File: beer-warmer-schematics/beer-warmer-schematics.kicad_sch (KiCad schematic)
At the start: 20 parts, among them J1 USB_C_Receptacle_USB2.0_14P, J2 Screw_Terminal_01x02, J3 Conn_01x07_Socket, J4 Conn_01x07_Socket, J5 Conn_01x04_Pin, J6 Screw_Terminal_01x03, Q1 AOD4184A, U2 LM2596S-5, U3 CH224K

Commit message: initial routing
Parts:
- added FID1, FID2, FID3: Fiducial, Fiducial:Fiducial_0.5mm_Mask1.5mm, symbol Mechanical:Fiducial
- added H1, H2, H3, H4: MountingHole, MountingHole:MountingHole_3.2mm_M3, symbol Mechanical:MountingHole
- added R5: 10K, Resistor_SMD:R_0201_0603Metric, symbol Device:R
- U1: footprint (none) -> Library:XIAO-ESP32C6-DIP
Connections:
- net +5V: now also U1.14 (5V); no longer U1.13 (5V)
- net D0: now also U1.1 (D0); no longer U1.0 (D0)
- net D1: now also U1.2 (D1); no longer U1.1 (D1)
- net GND: now also U1.13 (GND); no longer U1.12 (GND), U3.8 (VBUS)
- net SCL: now also U1.6 (D5); no longer U1.5 (D5)
- net SDA: now also U1.5 (D4); no longer U1.4 (D4)
- net at U1.10 (D9): now also J3.5 (Pin_5); no longer J3.4 (Pin_4)
- net at U1.11 (D10): now also J3.4 (Pin_4); no longer J3.3 (Pin_3)
- net at U1.3 (D2): now also J4.5 (Pin_5); no longer J4.4 (Pin_4)
- net at J4.1 (Pin_1): now also U1.7 (D6); no longer U1.6 (D6)
- net at J3.7 (Pin_7): now also U1.8 (D7); no longer U1.7 (D7)
- net at J3.6 (Pin_6): now also U1.9 (D8); no longer U1.8 (D8)
- net at J1.A4 (VBUS), J1.A9 (VBUS), J1.B4 (VBUS)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: now also R5.1
- new net: R5.2, U3.8 (VBUS)
- new net: J3.3 (Pin_3), U1.12 (3V3)
- new net: J4.4 (Pin_4), U1.4 (D3)
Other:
- moved on the sheet: C1, R1

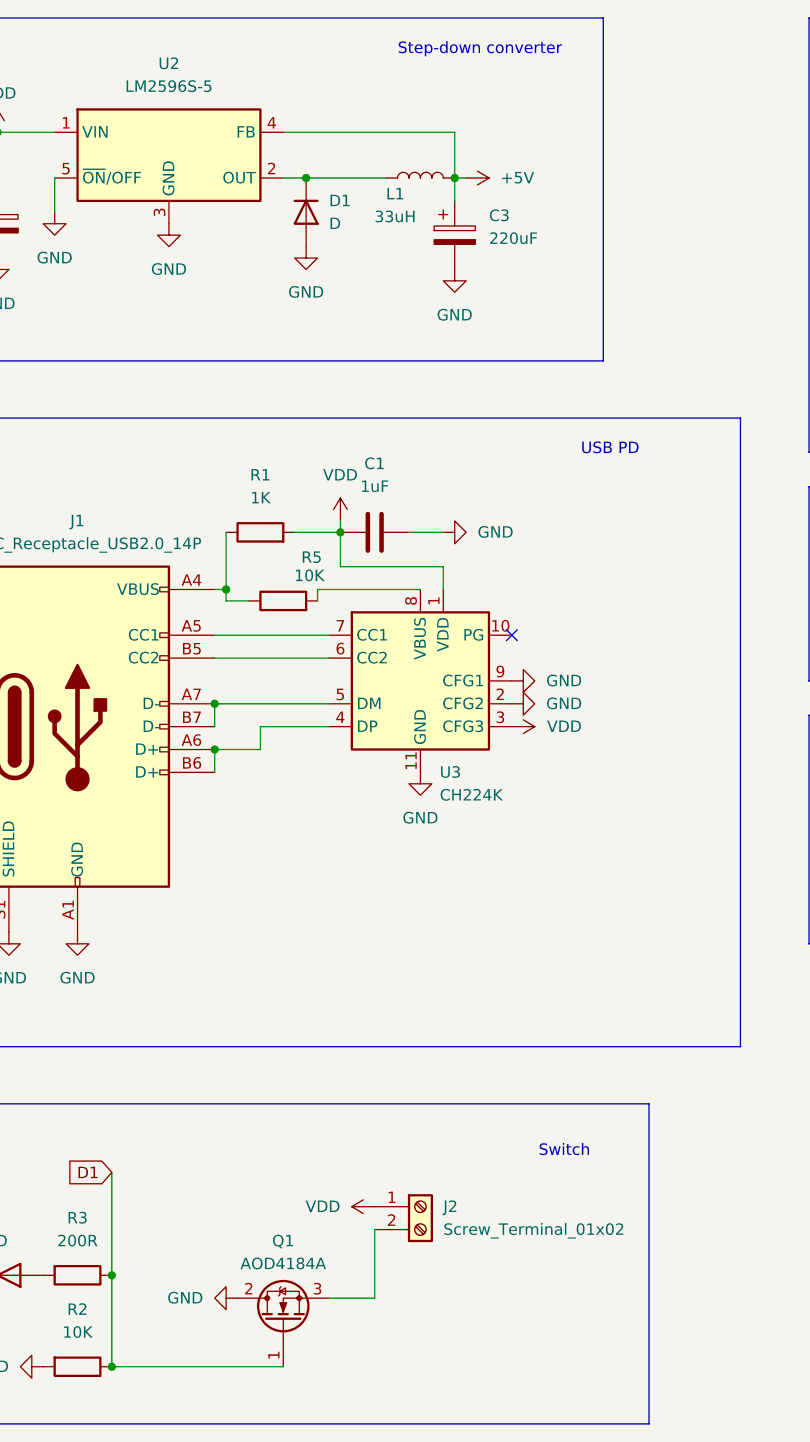
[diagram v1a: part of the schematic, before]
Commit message: cleanup add more lcsc numbers
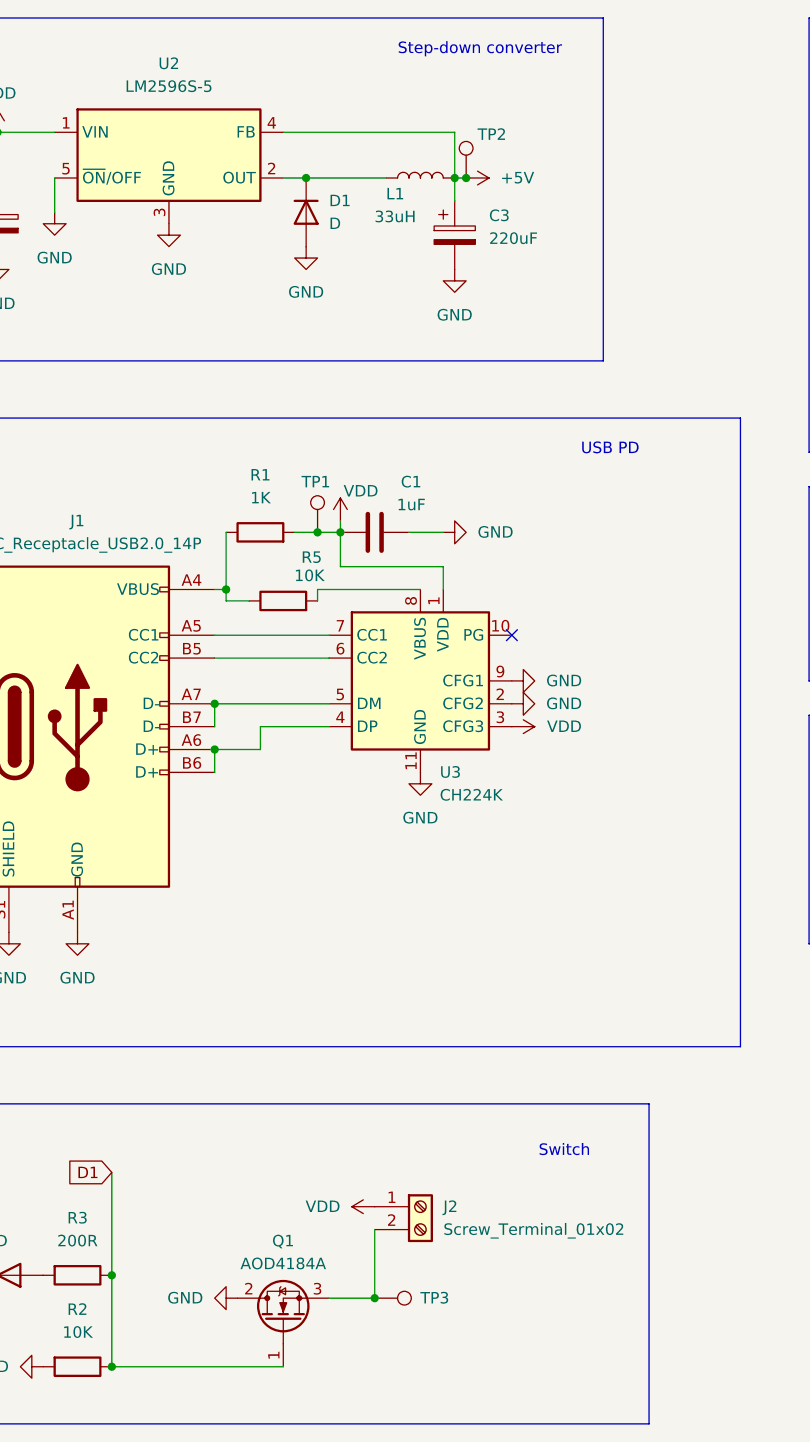
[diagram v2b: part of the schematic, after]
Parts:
- added TP1, TP2, TP3: TestPoint, TestPoint:TestPoint_Pad_D1.0mm, symbol Connector:TestPoint
- D2: LCSC (none) -> C2286
- J3, J4: LCSC (none) -> C2932672
- J5: LCSC (none) -> C594232
- Q1: LCSC (none) -> C99124
- R1: LCSC (none) -> C22548
- R3: LCSC C15401 -> C8218
- U2: LCSC (none) -> C5276750
- U3: LCSC (none) -> C970725
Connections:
- net +5V: now also TP2.1
- net VDD: now also TP1.1
- net at J2.2 (Pin_2), Q1.3 (S): now also TP3.1

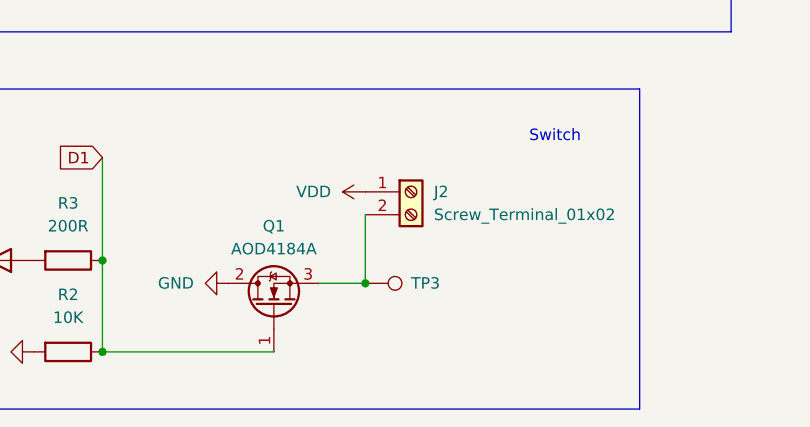
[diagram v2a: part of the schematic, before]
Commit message: redid board layout
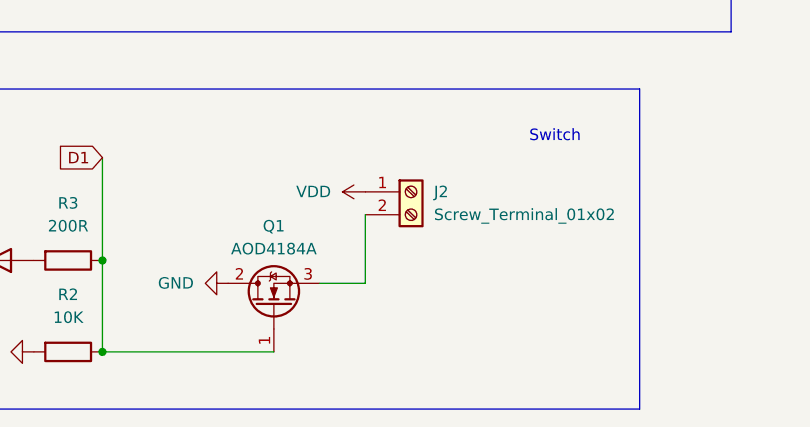
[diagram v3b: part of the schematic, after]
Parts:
- removed TP3: TestPoint, TestPoint:TestPoint_Pad_D1.0mm, symbol Connector:TestPoint
- H1, H2, H3, H4: footprint MountingHole:MountingHole_3.2mm_M3 -> MountingHole:MountingHole_3.2mm_M3_DIN965_Pad
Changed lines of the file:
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@@
 	)
 	(junction
-		(at 83.82 160.02)
-		(diameter 0)
-		(color 0 0 0 0)
-	)
-	(junction
 		(at 41.91 30.48)
 		(diameter 0)
@@
 	)
 	(symbol
-		(lib_id "Connector:TestPoint")
-		(at 83.82 160.02 270)
-		(unit 1)
-		(exclude_from_sim no)
-		(in_bom yes)
-		(on_board yes)
-		(dnp no)
-		(property "Reference" "TP3"
-			(at 88.9 160.02 90)
-			(effects
-				(font
-					(size 1.27 1.27)
-				)
-				(justify left)
-			)
-		)
-		(property "Value" "TestPoint"
-			(at 88.9 161.2899 90)
-			(effects
-				(font
-					(size 1.27 1.27)
-				)
-				(justify left)
-				(hide yes)
-			)
-		)
-		(property "Footprint" "TestPoint:TestPoint_Pad_D1.0mm"
-			(at 83.82 165.1 0)
-			(effects
-				(font
-					(size 1.27 1.27)
-				)
-				(hide yes)
-			)
-		)
-		(property "Datasheet" "~"
-			(at 83.82 165.1 0)
-			(effects
-				(font
-					(size 1.27 1.27)
-				)
-				(hide yes)
-			)
-		)
-		(property "Description" "test point"
-			(at 83.82 160.02 0)
-			(effects
-				(font
-					(size 1.27 1.27)
-				)
-				(hide yes)
-			)
-		)
-		(pin "1"
-		)
-		(instances
-			(project ""
-				(path "/70572ac2-8723-48b8-abb1-12d225a3bb68"
-					(reference "TP3")
-					(unit 1)
-				)
-			)
-		)
-	)
-	(symbol
 		(lib_id "power:GND")
 		(at 143.51 100.33 270)
@@
 			)
 		)
-		(property "Footprint" "MountingHole:MountingHole_3.2mm_M3"
+		(property "Footprint" "MountingHole:MountingHole_3.2mm_M3_DIN965_Pad"
 			(at 208.28 111.76 0)
 			(effects
@@
 			)
 		)
-		(property "Footprint" "MountingHole:MountingHole_3.2mm_M3"
+		(property "Footprint" "MountingHole:MountingHole_3.2mm_M3_DIN965_Pad"
 			(at 208.28 105.41 0)
 			(effects
@@
 			)
 		)
-		(property "Footprint" "MountingHole:MountingHole_3.2mm_M3"
+		(property "Footprint" "MountingHole:MountingHole_3.2mm_M3_DIN965_Pad"
 			(at 208.28 92.71 0)
 			(effects
@@
 			)
 		)
-		(property "Footprint" "MountingHole:MountingHole_3.2mm_M3"
+		(property "Footprint" "MountingHole:MountingHole_3.2mm_M3_DIN965_Pad"
 			(at 208.28 99.06 0)
 			(effects

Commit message: fix screw terminal component
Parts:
- J2: footprint TerminalBlock_Phoenix:TerminalBlock_Phoenix_MKDS-1,5-2_1x02_P5.00mm_Horizontal -> TerminalBlock_Phoenix:TerminalBlock_Phoenix_MKDS-1,5-2-5.08_1x02_P5.08mm_Horizontal; LCSC C128027 -> C8465
- J6: footprint TerminalBlock_Phoenix:TerminalBlock_Phoenix_MKDS-1,5-3_1x03_P5.00mm_Horizontal -> TerminalBlock_Phoenix:TerminalBlock_Phoenix_MKDS-1,5-3-5.08_1x03_P5.08mm_Horizontal; LCSC C128026 -> C72334
- TP1, TP2: now left out of the parts list
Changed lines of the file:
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@@
 		(unit 1)
 		(exclude_from_sim no)
-		(in_bom yes)
+		(in_bom no)
 		(on_board yes)
 		(dnp no)
@@
 		(unit 1)
 		(exclude_from_sim no)
-		(in_bom yes)
+		(in_bom no)
 		(on_board yes)
 		(dnp no)
@@
 			)
 		)
-		(property "Footprint" "TerminalBlock_Phoenix:TerminalBlock_Phoenix_MKDS-1,5-2_1x02_P5.00mm_Horizontal"
+		(property "Footprint" "TerminalBlock_Phoenix:TerminalBlock_Phoenix_MKDS-1,5-2-5.08_1x02_P5.08mm_Horizontal"
 			(at 88.9 149.86 0)
 			(effects
@@
 			)
 		)
-		(property "LCSC" "C128027"
+		(property "LCSC" "C8465"
 			(at 88.9 149.86 0)
 			(effects
@@
 			)
 		)
-		(property "Footprint" "TerminalBlock_Phoenix:TerminalBlock_Phoenix_MKDS-1,5-3_1x03_P5.00mm_Horizontal"
+		(property "Footprint" "TerminalBlock_Phoenix:TerminalBlock_Phoenix_MKDS-1,5-3-5.08_1x03_P5.08mm_Horizontal"
 			(at 158.75 102.87 0)
 			(effects
@@
 			)
 		)
-		(property "LCSC" "C128026"
+		(property "LCSC" "C72334"
 			(at 158.75 102.87 0)
 			(effects

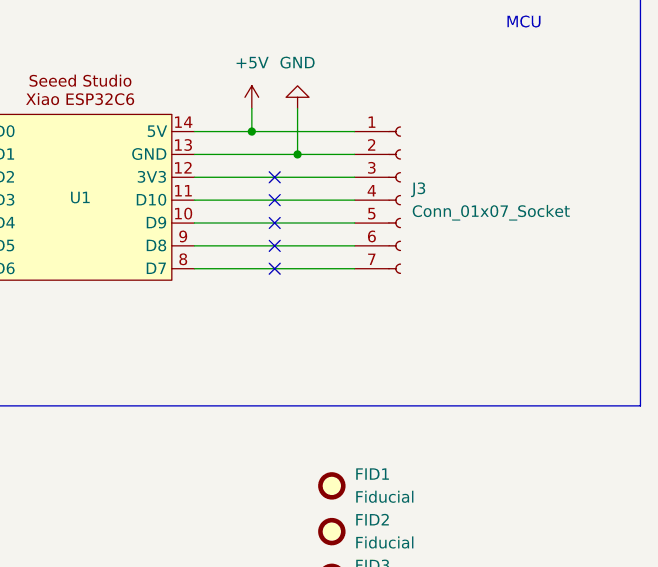
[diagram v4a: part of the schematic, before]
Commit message: power indicator
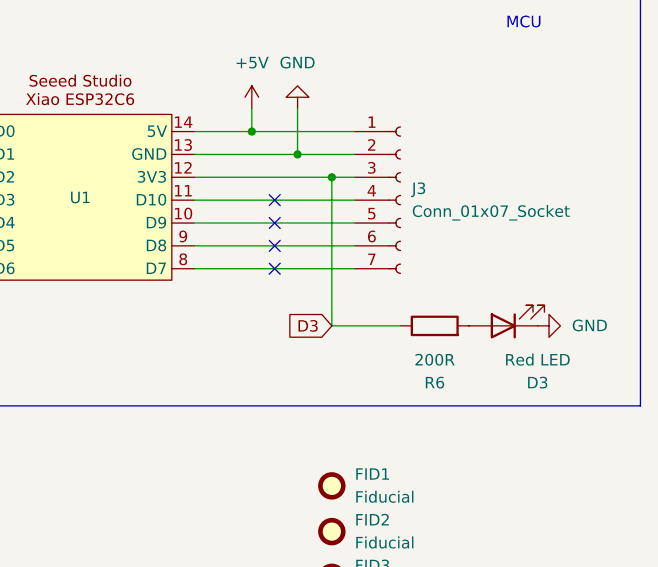
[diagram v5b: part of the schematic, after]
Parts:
- added D3: Red LED, Resistor_SMD:R_0201_0603Metric, symbol Device:LED
- added R6: 200R, Resistor_SMD:R_0201_0603Metric, symbol Device:R
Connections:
- net GND: now also D3.1 (K)
- net D3: now reaches J3.3 (Pin_3), U1.12 (3V3)
- net D3: now also R6.1
- new net: D3.2 (A), R6.2
- no-connect marks 9 -> 8

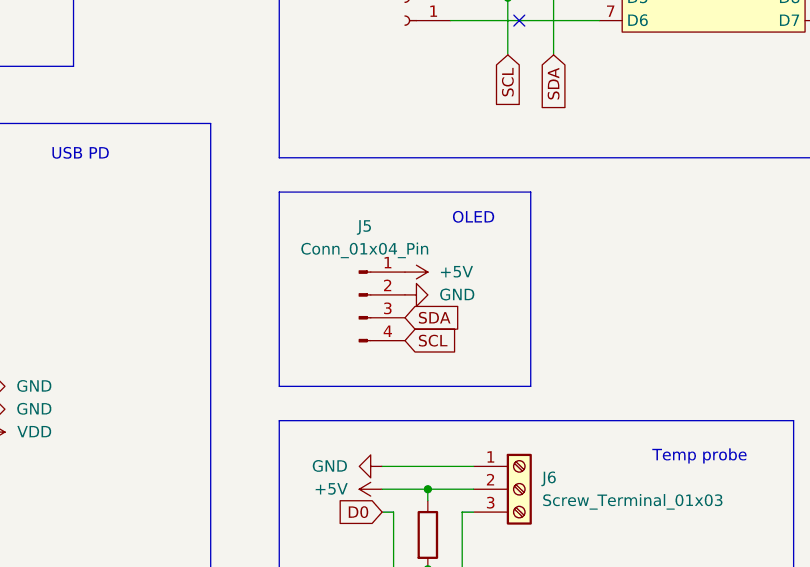
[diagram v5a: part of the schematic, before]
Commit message: use more standard components
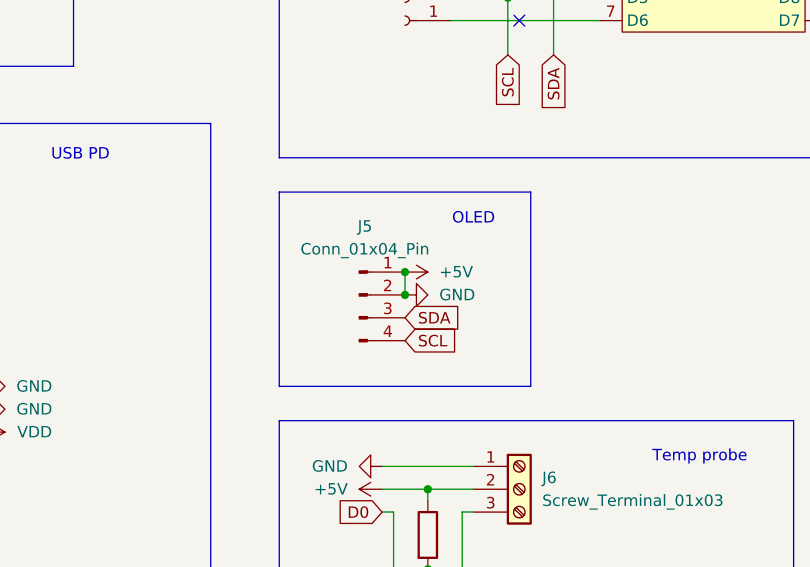
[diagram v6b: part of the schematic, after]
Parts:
- C1: footprint Capacitor_SMD:C_0201_0603Metric -> Capacitor_SMD:CP_Elec_10x10.5; LCSC C1592 -> C7471898
- C2: footprint Capacitor_THT:CP_Radial_D10.0mm_P5.00mm -> Capacitor_SMD:CP_Elec_10x10.5; LCSC C323859 -> C7471898
- C3: footprint Capacitor_THT:CP_Radial_D6.3mm_P2.50mm -> Capacitor_SMD:CP_Elec_6.3x7.7; LCSC C43340 -> C3342
- D1: LCSC C2102 -> C8598
- L1: footprint Library:IND_BOURNS_SRR1280 -> Inductor_SMD:L_SXN_SMDRI127; LCSC C2045204 -> C9400
- R1: footprint Resistor_SMD:R_0201_0603Metric -> Resistor_SMD:R_1206_3216Metric; LCSC C22548 -> C4410
- R2, R4, R5: footprint Resistor_SMD:R_0201_0603Metric -> Resistor_SMD:R_1206_3216Metric; LCSC C15401 -> C17902
- R3, R6: LCSC C8218 -> C22962
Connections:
- net GND is gone; now on net +5V: C1.2, C2.2, C3.2, D1.2 (A), D2.1 (K), D3.1 (K), J1.A1 (GND), J1.A12 (GND), J1.B1 (GND), J1.B12 (GND), J1.S1 (SHIELD), J3.2 (Pin_2), J5.2 (Pin_2), J6.1 (Pin_1), Q1.2 (D), R2.2, U1.13 (GND), U2.3 (GND), U2.5 (~{ON}/OFF), U3.11 (GND), U3.2 (CFG2), U3.9 (CFG1)
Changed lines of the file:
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@@
 	)
 	(junction
+		(at 146.05 78.74)
+		(diameter 0)
+		(color 0 0 0 0)
+	)
+	(junction
 		(at 157.48 35.56)
 		(diameter 0)
@@
 	)
 	(junction
+		(at 146.05 81.28)
+		(diameter 0)
+		(color 0 0 0 0)
+	)
+	(junction
 		(at 199.39 35.56)
 		(diameter 0)
@@
 	(wire
 		(pts
+			(xy 146.05 78.74) (xy 146.05 81.28)
+		)
+		(stroke
+			(width 0)
+			(type default)
+		)
+	)
+	(wire
+		(pts
 			(xy 73.66 30.48) (xy 92.71 30.48)
 		)
@@
 			)
 		)
-		(property "Footprint" "Resistor_SMD:R_0201_0603Metric"
+		(property "Footprint" "Resistor_SMD:R_1206_3216Metric"
 			(at 73.66 84.328 90)
 			(effects
@@
 			)
 		)
-		(property "LCSC" "C15401"
+		(property "LCSC" "C17902"
 			(at 73.66 82.55 90)
 			(effects
@@
 			)
 		)
-		(property "LCSC" "C2102"
+		(property "LCSC" "C8598"
 			(at 76.2 39.37 90)
 			(effects
@@
 			)
 		)
-		(property "Footprint" "Capacitor_THT:CP_Radial_D6.3mm_P2.50mm"
+		(property "Footprint" "Capacitor_SMD:CP_Elec_6.3x7.7"
 			(at 93.6752 45.72 0)
 			(effects
@@
 			)
 		)
-		(property "LCSC" "C43340"
+		(property "LCSC" "C3342"
 			(at 92.71 41.91 0)
 			(effects
@@
 			)
 		)
-		(property "Footprint" "Resistor_SMD:R_0201_0603Metric"
+		(property "Footprint" "Resistor_SMD:R_1206_3216Metric"
 			(at 50.8 165.862 90)
 			(effects
@@
 			)
 		)
-		(property "LCSC" "C15401"
+		(property "LCSC" "C17902"
 			(at 50.8 167.64 90)
 			(effects
@@
 			)
 		)
-		(property "LCSC" "C8218"
+		(property "LCSC" "C22962"
 			(at 219.71 57.15 90)
 			(effects
@@
 			)
 		)
-		(property "Footprint" "Capacitor_THT:CP_Radial_D10.0mm_P5.00mm"
+		(property "Footprint" "Capacitor_SMD:CP_Elec_10x10.5"
 			(at 42.8752 44.45 0)
 			(effects
@@
 			)
 		)
-		(property "LCSC" "C323859"
+		(property "LCSC" "C7471898"
 			(at 41.91 40.64 0)
 			(effects
@@
 			)
 		)
-		(property "LCSC" "C8218"
+		(property "LCSC" "C22962"
 			(at 50.8 157.48 90)
 			(effects
@@
 			)
 		)
-		(property "Footprint" "Capacitor_SMD:C_0201_0603Metric"
+		(property "Footprint" "Capacitor_SMD:CP_Elec_10x10.5"
 			(at 87.63 73.9648 0)
 			(effects
@@
 			)
 		)
-		(property "LCSC" "C1592"
+		(property "LCSC" "C7471898"
 			(at 83.82 74.93 90)
 			(effects
@@
 			)
 		)
-		(property "Footprint" "Library:IND_BOURNS_SRR1280"
+		(property "Footprint" "Inductor_SMD:L_SXN_SMDRI127"
 			(at 88.9 35.56 0)
 			(effects
@@
 			)
 		)
-		(property "LCSC" "C2045204"
+		(property "LCSC" "C9400"
 			(at 88.9 35.56 90)
 			(effects
@@
 			)
 		)
-		(property "Footprint" "Resistor_SMD:R_0201_0603Metric"
+		(property "Footprint" "Resistor_SMD:R_1206_3216Metric"
 			(at 71.12 76.708 90)
 			(effects
@@
 			)
 		)
-		(property "LCSC" "C22548"
+		(property "LCSC" "C4410"
 			(at 71.12 74.93 90)
 			(effects
@@
 			)
 		)
-		(property "Footprint" "Resistor_SMD:R_0201_0603Metric"
+		(property "Footprint" "Resistor_SMD:R_1206_3216Metric"
 			(at 146.812 107.95 90)
 			(effects
@@
 			)
 		)
-		(property "LCSC" "C15401"
+		(property "LCSC" "C17902"
 			(at 148.59 107.95 90)
 			(effects
